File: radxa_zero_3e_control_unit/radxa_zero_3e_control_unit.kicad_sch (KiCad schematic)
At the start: 39 parts, among them J14 DebugUART, J16 Malibotti, J17 Robot, J18 STLINK_V3_MINIE, J19 IO, J21 STDC14, J22 USB STM32, J23 IO, J24 IO, J3 TOF3, J4 TOF2, J5 TOF1, J6 TOF1, U2 STM32G431RBTx, X1 Radxa Zero 3E

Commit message: Various
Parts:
- added J25: IO, Connector_JST:JST_XH_B6B-XH-A_1x06_P2.50mm_Vertical, symbol Connector_Generic:Conn_01x06
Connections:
- net +3V3: now also J25.1 (Pin_1), J25.2 (Pin_2), J25.3 (Pin_3)
- net GND: now also J25.4 (Pin_4), J25.5 (Pin_5), J25.6 (Pin_6)

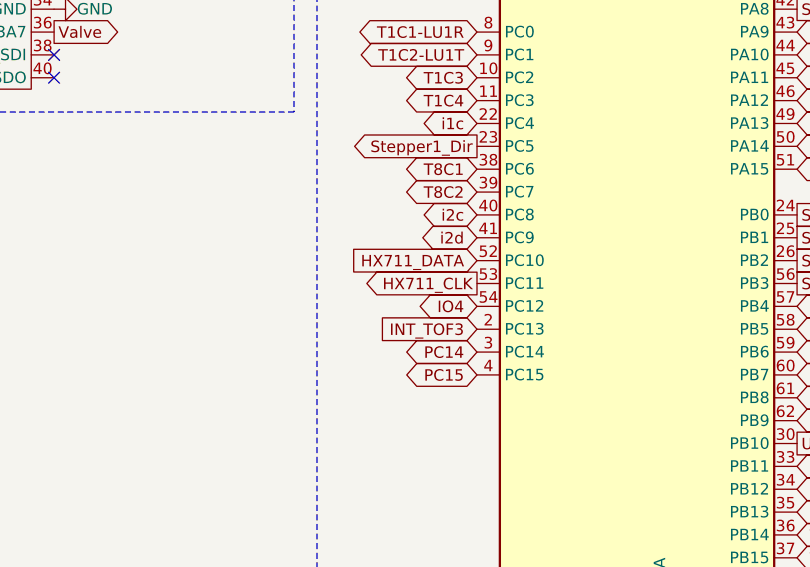
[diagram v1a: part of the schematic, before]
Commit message: Fixes
- air ventilation holes
- HX711 is on SPI MISO and SPI MOSI according to https://github.com/ufnalski/hx711_non_blocking_spi_g431kb (PC10-->PC11, PC11-->PC12)
- DC connector polarity changed
- connectors for voltages
- TMC2209 got different communication IDs
- Elkos mor space
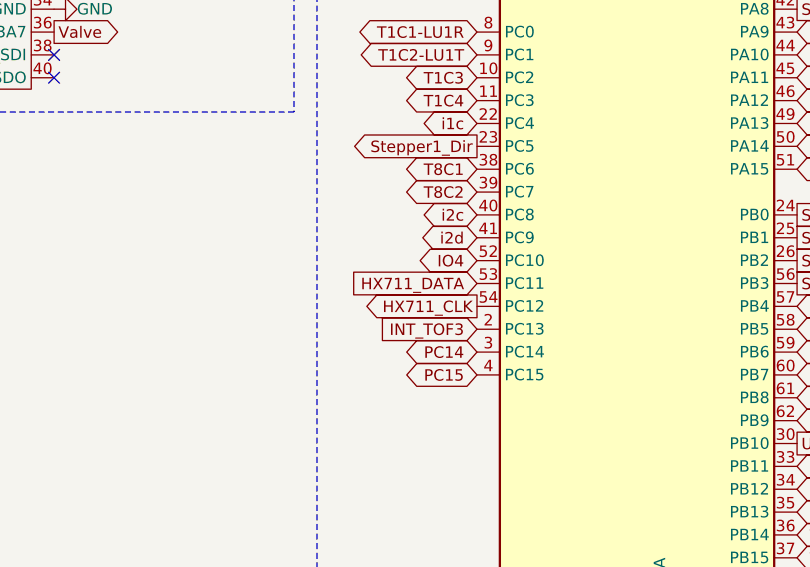
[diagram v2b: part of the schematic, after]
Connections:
- net HX711_CLK: now also U2.54 (PC12); no longer U2.53 (PC11)
- net HX711_DATA: now also U2.53 (PC11); no longer U2.52 (PC10)
- net IO4: now also U2.52 (PC10); no longer U2.54 (PC12)

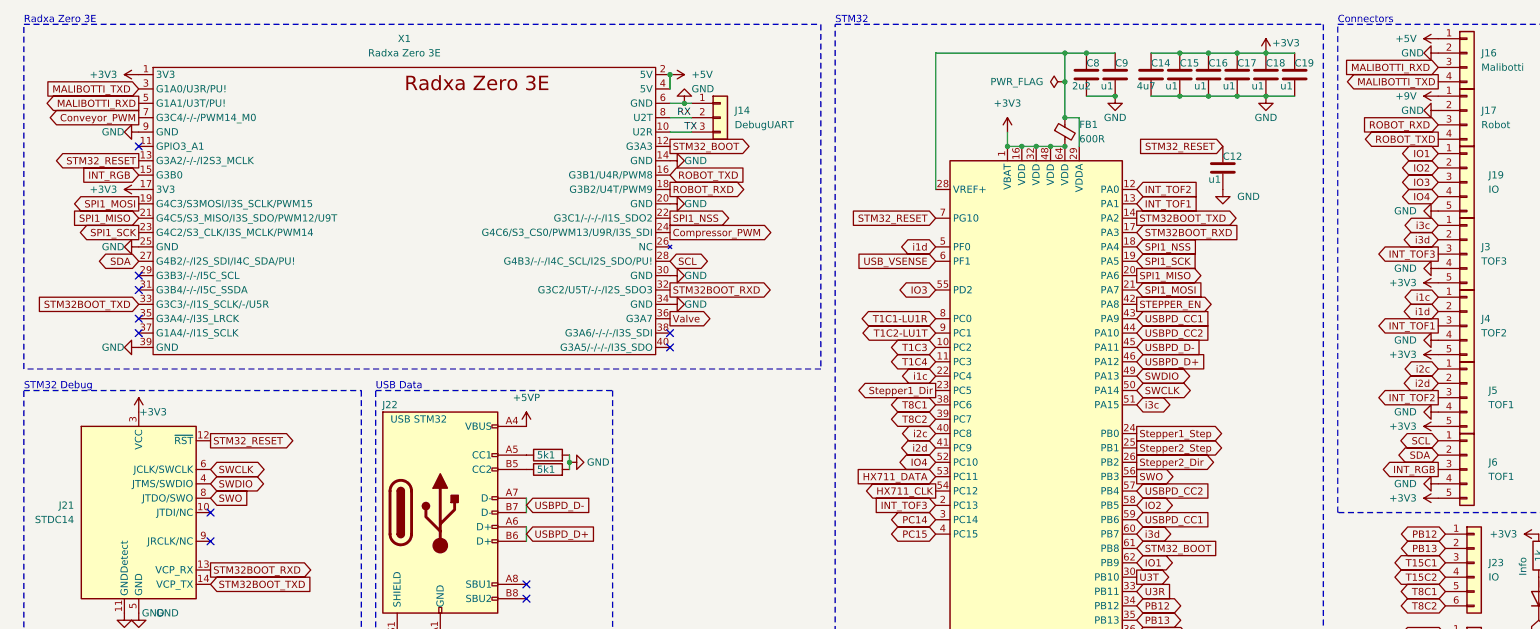
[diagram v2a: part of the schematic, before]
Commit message: WIP, before repinning SUM32G431
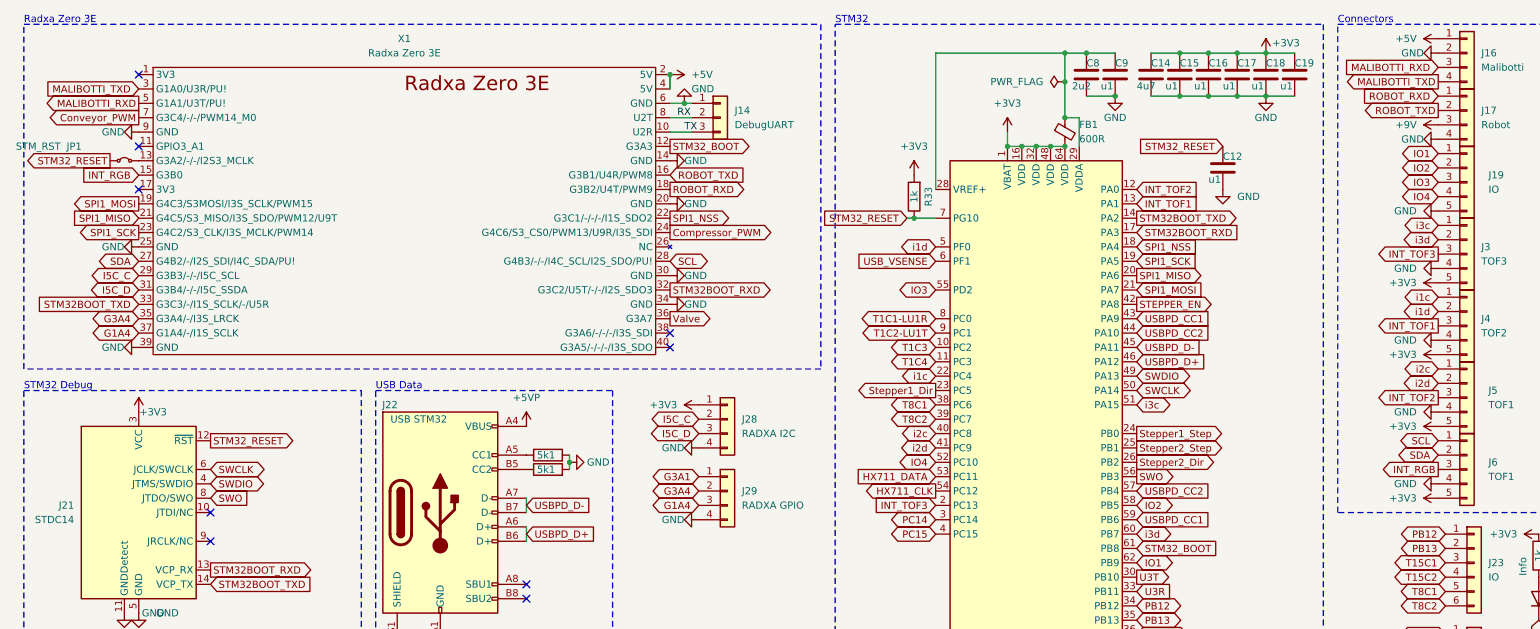
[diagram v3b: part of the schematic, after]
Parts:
- added J28: RADXA I2C, Connector_JST:JST_XH_B4B-XH-A_1x04_P2.50mm_Vertical, symbol Connector_Generic:Conn_01x04
- added J29: RADXA GPIO, Connector_JST:JST_XH_B4B-XH-A_1x04_P2.50mm_Vertical, symbol Connector_Generic:Conn_01x04
- added JP1: STM_RST, Jumper:SolderJumper-2_P1.3mm_Bridged2Bar_RoundedPad1.0x1.5mm, symbol Jumper:Jumper_2_Small_Bridged
- added R33: 1k, Resistor_SMD:R_0402_1005Metric, symbol Device:R
- J17: footprint liebler_CONN:JST_XH_S4B-XH-A-1_1x04_P2.50mm_Horizontal_SmallerCourtyard -> Connector_JST:JST_XH_B4B-XH-A_1x04_P2.50mm_Vertical
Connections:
- net +3V3: now also J28.1 (Pin_1), R33.2; no longer X1.1 (3V3), X1.17 (3V3)
- net +9V: now also J17.3 (Pin_3); no longer J17.1 (Pin_1)
- net GND: now also J17.4 (Pin_4), J28.4 (Pin_4), J29.4 (Pin_4); no longer J17.2 (Pin_2)
- net ROBOT_RXD: now also J17.1 (Pin_1); no longer J17.3 (Pin_3)
- net ROBOT_TXD: now also J17.2 (Pin_2); no longer J17.4 (Pin_4)
- net STM32_RESET: now also JP1.1 (A), R33.1; no longer X1.13 (G3A2/-/-/I2S3_MCLK)
- net I5C_C: now reaches X1.29 (G3B3/-/-/I5C_SCL)
- net I5C_C: now also J28.2 (Pin_2)
- net I5C_D: now reaches X1.31 (G3B4/-/-/I5C_SSDA)
- net I5C_D: now also J28.3 (Pin_3)
- net G3A4: now reaches X1.35 (G3A4/-/I3S_LRCK)
- net G3A4: now also J29.2 (Pin_2)
- net G1A4: now reaches X1.37 (G1A4/-/I1S_SCLK)
- net G1A4: now also J29.3 (Pin_3)
- new net: JP1.2 (B), X1.13 (G3A2/-/-/I2S3_MCLK)
- new net G3A1: J29.1 (Pin_1)
- no-connect marks 13 -> 11

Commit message: Udated control unit pcb
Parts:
- removed J17: Robot, Connector_JST:JST_XH_B4B-XH-A_1x04_P2.50mm_Vertical, symbol Connector_Generic:Conn_01x04
- removed J18: STLINK_V3_MINIE, Connector_IDC:IDC-Header_2x05_P2.54mm_Vertical, symbol Connector_Generic:Conn_02x05_Odd_Even
- removed J19: IO, Connector_JST:JST_XH_S5B-XH-A-1_1x05_P2.50mm_Horizontal, symbol Connector_Generic:Conn_01x05
- removed J23, J24, J25: IO, Connector_JST:JST_XH_B6B-XH-A_1x06_P2.50mm_Vertical, symbol Connector_Generic:Conn_01x06
- removed J28: RADXA I2C, Connector_JST:JST_XH_B4B-XH-A_1x04_P2.50mm_Vertical, symbol Connector_Generic:Conn_01x04
- removed J29: RADXA GPIO, Connector_JST:JST_XH_B4B-XH-A_1x04_P2.50mm_Vertical, symbol Connector_Generic:Conn_01x04
- added C41: u1, Capacitor_SMD:C_0402_1005Metric, symbol Device:C
- added H3, H4: M2,5, MountingHole:MountingHole_2.7mm, symbol Mechanical:MountingHole
- added J11: Raspberry_Pi_5, liebler_MODULES:RasPi5, symbol Connector:Raspberry_Pi_4
- added J12: CAN, liebler_CONN:JST_XH_B3B-XH-A_1x03_P2.50mm_Vertical_smaller, symbol Connector_Generic:Conn_01x03
- added J30: LightBarrier1, liebler_CONN:JST_XH_B3B-XH-A_1x03_P2.50mm_Vertical_smaller, symbol Connector_Generic:Conn_01x03
- added J31: LightBarrier2, liebler_CONN:JST_XH_B3B-XH-A_1x03_P2.50mm_Vertical_smaller, symbol Connector_Generic:Conn_01x03
- added J32: LightBarrier3, liebler_CONN:JST_XH_B3B-XH-A_1x03_P2.50mm_Vertical_smaller, symbol Connector_Generic:Conn_01x03
- added J33: PressureTransducer, liebler_CONN:JST_XH_B3B-XH-A_1x03_P2.50mm_Vertical_smaller, symbol Connector_Generic:Conn_01x03
- added JP2, JP3, JP4: 5-24, Jumper:SolderJumper-3_P1.3mm_Open_RoundedPad1.0x1.5mm_NumberLabels, symbol Jumper:SolderJumper_3_Open
- added M1: W5500_mini, liebler_MODULES:W5500-mini, symbol liebler_MODULES:W5500_mini
- added M2: FanMech, liebler_MECH:FAN2507, symbol Motor:Fan
- added M3: FanElek, Connector_JST:JST_XH_B2B-XH-A_1x02_P2.50mm_Vertical, symbol Motor:Fan
- added R32, R34, R35: 10k, Resistor_SMD:R_0402_1005Metric, symbol Device:R
- added R36: 1k, Resistor_SMD:R_0402_1005Metric, symbol Device:R
- added U7: SIT3051TK, Package_DFN_QFN:DFN-8-1EP_3x3mm_P0.65mm_EP1.55x2.4mm, symbol liebler_SEMICONDUCTORS:SIT3051TK
- C12, C15, C16, C17, C18, C19, C9: footprint Capacitor_SMD:C_0201_0603Metric -> Capacitor_SMD:C_0402_1005Metric
- H6: footprint MountingHole:MountingHole_3.2mm_M3 -> MountingHole:MountingHole_2.7mm
- J16: footprint liebler_CONN:JST_XH_S4B-XH-A-1_1x04_P2.50mm_Horizontal_SmallerCourtyard -> liebler_CONN:JST_XH_B4B-XH-A_1x04_P2.50mm_Vertical_smaller
- J3, J4, J5: footprint Connector_JST:JST_XH_S5B-XH-A-1_1x05_P2.50mm_Horizontal -> liebler_CONN:JST_XH_B5B-XH-A_1x05_P2.50mm_Vertical_smaller
- J6: value TOF1 -> RGB; footprint Connector_JST:JST_XH_S5B-XH-A-1_1x05_P2.50mm_Horizontal -> liebler_CONN:JST_XH_B5B-XH-A_1x05_P2.50mm_Vertical_smaller
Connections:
- net HX711_CLK is gone; now on net INT_TOF1: U2.54 (PC12)
- net IO2 is gone; now on net INT_TOF2: U2.58 (PB5)
- net IO3 is gone; now on net INT_RGB: U2.55 (PD2)
- net PB13 is gone; now on net STEPPER_EN: U2.35 (PB13)
- net PC15 is gone; now on net INT_TOF3: U2.4 (PC15)
- net +3V3: now also C41.1, M1.10 (3V3), M1.11 (3V3), U7.3 (VCC)
- net +5V: now also J16.4 (Pin_4), J33.2 (Pin_2), JP2.1 (A), JP3.1 (A), JP4.1 (A), M3.1 (+); no longer J16.1 (Pin_1)
- net GND: now also J16.3 (Pin_3), C41.2, J12.2 (Pin_2), J30.3 (Pin_3), J31.3 (Pin_3), J32.3 (Pin_3), J33.3 (Pin_3), M1.1 (GND), M1.12 (GND), M1.2 (GND), M3.2 (-), R34.1, R35.1, U7.2 (GND), U7.9 (PAD); no longer J16.2 (Pin_2)
- net INT_RGB: no longer X1.15 (G3B0)
- net INT_TOF1: now also J5.3 (Pin_3); no longer J4.3 (Pin_3), U2.13 (PA1)
- net INT_TOF2: now also J4.3 (Pin_3); no longer J5.3 (Pin_3), U2.12 (PA0)
- net INT_TOF3: no longer U2.2 (PC13)
- net SCL: no longer J6.1 (Pin_1)
- net SDA: no longer J6.2 (Pin_2)
- net SPI1_MISO: now also M1.7 (MISO)
- net SPI1_MOSI: now also M1.3 (MOSI)
- net SPI1_NSS: now also M1.5 (~{CS}[PU])
- net SPI1_SCK: now also M1.4 (SCLK)
- net STEPPER_EN: no longer U2.42 (PA8)
- net USB_VSENSE: now also U2.42 (PA8); no longer U2.6 (PF1)
- net at X1.13 (G3A2/-/-/I2S3_MCLK): no longer JP1.2 (B)
- net STM32_BOOT_CAN_RX: now reaches X1.38 (G3A6/-/-/-/I3S_SDI)
- net STM32_BOOT_CAN_RX: now also U2.61 (PB8), R36.2
- net Compressor_PWM: no longer names the net of X1.24 (G4C6/S3_CS0/PWM13/U9R/I3S_SDI)
- net Conveyor_PWM: no longer names the net of X1.7 (G3C4/-/-/PWM14_M0)
- net G1A4: no longer names the net of X1.37 (G1A4/-/I1S_SCLK)
- net G3A4: no longer names the net of X1.35 (G3A4/-/I3S_LRCK)
- net HX711_DATA renamed ROBOT_U4R
- net I5C_C: no longer names the net of X1.29 (G3B3/-/-/I5C_SCL)
- net I5C_D: no longer names the net of X1.31 (G3B4/-/-/I5C_SSDA)
- net IO1 renamed CAN_TX
- net CAN_TX: now also U7.4 (R)
- net IO4 renamed ROBOT_U4T
- net MALIBOTTI_RXD: no longer names the net of X1.5 (G1A1/U3T/PU!)
- net MALIBOTTI_RXD: no longer J16.3 (Pin_3)
- net MALIBOTTI_TXD: no longer names the net of X1.3 (G1A0/U3R/PU!)
- net MALIBOTTI_TXD: no longer J16.4 (Pin_4)
- net PB12 renamed ADC1_IN11
- net PC14 renamed LightBarrier2
- net LightBarrier2: now also J31.1 (Pin_1)
- net ROBOT_RXD: no longer names the net of X1.18 (G3B2/U4T/PWM9)
- net ROBOT_TXD: no longer names the net of X1.16 (G3B1/U4R/PWM8)
- net STM32_BOOT: no longer names the net of X1.12 (G3A3)
- net STM32_BOOT: no longer U2.61 (PB8)
- net Stepper1_Dir renamed VALVE
- net Stepper1_Step renamed STEPPER1_DIR
- net Stepper2_Dir renamed ADC2_12
- net Stepper2_Step renamed STEPPER1_STEP
- net T15C1 renamed HX711_SPI2_MISO
- net T15C2 renamed HX711_SPI2_MOSI
- net T1C1-LU1R renamed MALIBOTTI_U1R
- net MALIBOTTI_U1R: now also J16.1 (Pin_1)
- net T1C2-LU1T renamed MALIBOTTI_U1T
- net MALIBOTTI_U1T: now also J16.2 (Pin_2)
- net T1C3 renamed PRESSURE_ADC
- net PRESSURE_ADC: now also R32.1, R34.2
- net T1C4 renamed W5500_IRQ
- net W5500_IRQ: now also M1.6 (~{INT}[PU])
- net T8C1 renamed STEPPER2_DIR_T3C1_T8C1
- net T8C2 renamed STEPPER2_STEP_T3C2_T8C2
- net Valve: no longer names the net of X1.36 (G3A7)
- net Valve: now also JP1.2 (B)
- net i1c renamed I2C2_SCL
- net i1d renamed I2C2_SDA
- net i2c renamed I2C1_SCL
- net I2C1_SCL: now also J6.1 (Pin_1), U2.51 (PA15); no longer U2.40 (PC8)
- net i2d renamed I2C1_SDA
- net I2C1_SDA: now also J6.2 (Pin_2), U2.60 (PB7); no longer U2.41 (PC9)
- net i3c renamed I2C3_SCL
- net I2C3_SCL: now also U2.40 (PC8); no longer U2.51 (PA15)
- net i3d renamed I2C3_SDA
- net I2C3_SDA: now also U2.41 (PC9); no longer U2.60 (PB7)
- new net: J30.2 (Pin_2), JP2.2 (C)
- new net: J32.2 (Pin_2), JP4.2 (C)
- new net: J31.2 (Pin_2), JP3.2 (C)
- new net: R35.2, U7.8 (Rs)
- new net: R36.1, U7.1 (D)
- new net: J33.1 (Pin_1), R32.2
- new net: J11.1 (3V3), J11.17 (3V3)
- new net: J11.14 (GND), J11.20 (GND), J11.25 (GND), J11.30 (GND), J11.34 (GND), J11.39 (GND), J11.6 (GND), J11.9 (GND)
- new net: J11.2 (5V), J11.4 (5V)
- new net +24V: JP2.3 (B), JP3.3 (B), JP4.3 (B)
- new net CANH: J12.1 (Pin_1), U7.7 (CANH)
- new net CANL: J12.3 (Pin_3), U7.6 (CANL)
- new net COMPRESSOR_T2C1: U2.12 (PA0)
- new net CONVEYOR_T2C2: U2.13 (PA1)
- new net LightBarrier1: J30.1 (Pin_1), U2.6 (PF1)
- new net LightBarrier3: J32.1 (Pin_1), U2.2 (PC13)
- no-connect marks 11 -> 9
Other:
- moved on the sheet: JP1

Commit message: Sigmoid Stepper
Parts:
- added R38, R39, R40, R41, R42, R43: 5k1, Resistor_SMD:R_0201_0603Metric, symbol Device:R
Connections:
- net +3V3: now also R38.1, R39.1, R40.1, R41.1, R42.1, R43.1
- net I2C1_SCL: now also R43.2
- net I2C1_SDA: now also R42.2
- net I2C2_SCL: now also R41.2
- net I2C2_SDA: now also R40.2
- net I2C3_SCL: now also R39.2
- net I2C3_SDA: now also R38.2
